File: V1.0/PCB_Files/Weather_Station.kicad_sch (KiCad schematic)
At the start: 39 parts, among them J1 N091-2832TSWFG02-H14, J2 USB_B_Micro, J3 Conn_01x04_Pin, U1 STM32F103C8T6, U2 HDC1080DMBR, U3 AMS1117-3.3, U5 SRV05-4, Y1 X322516MLB4SI

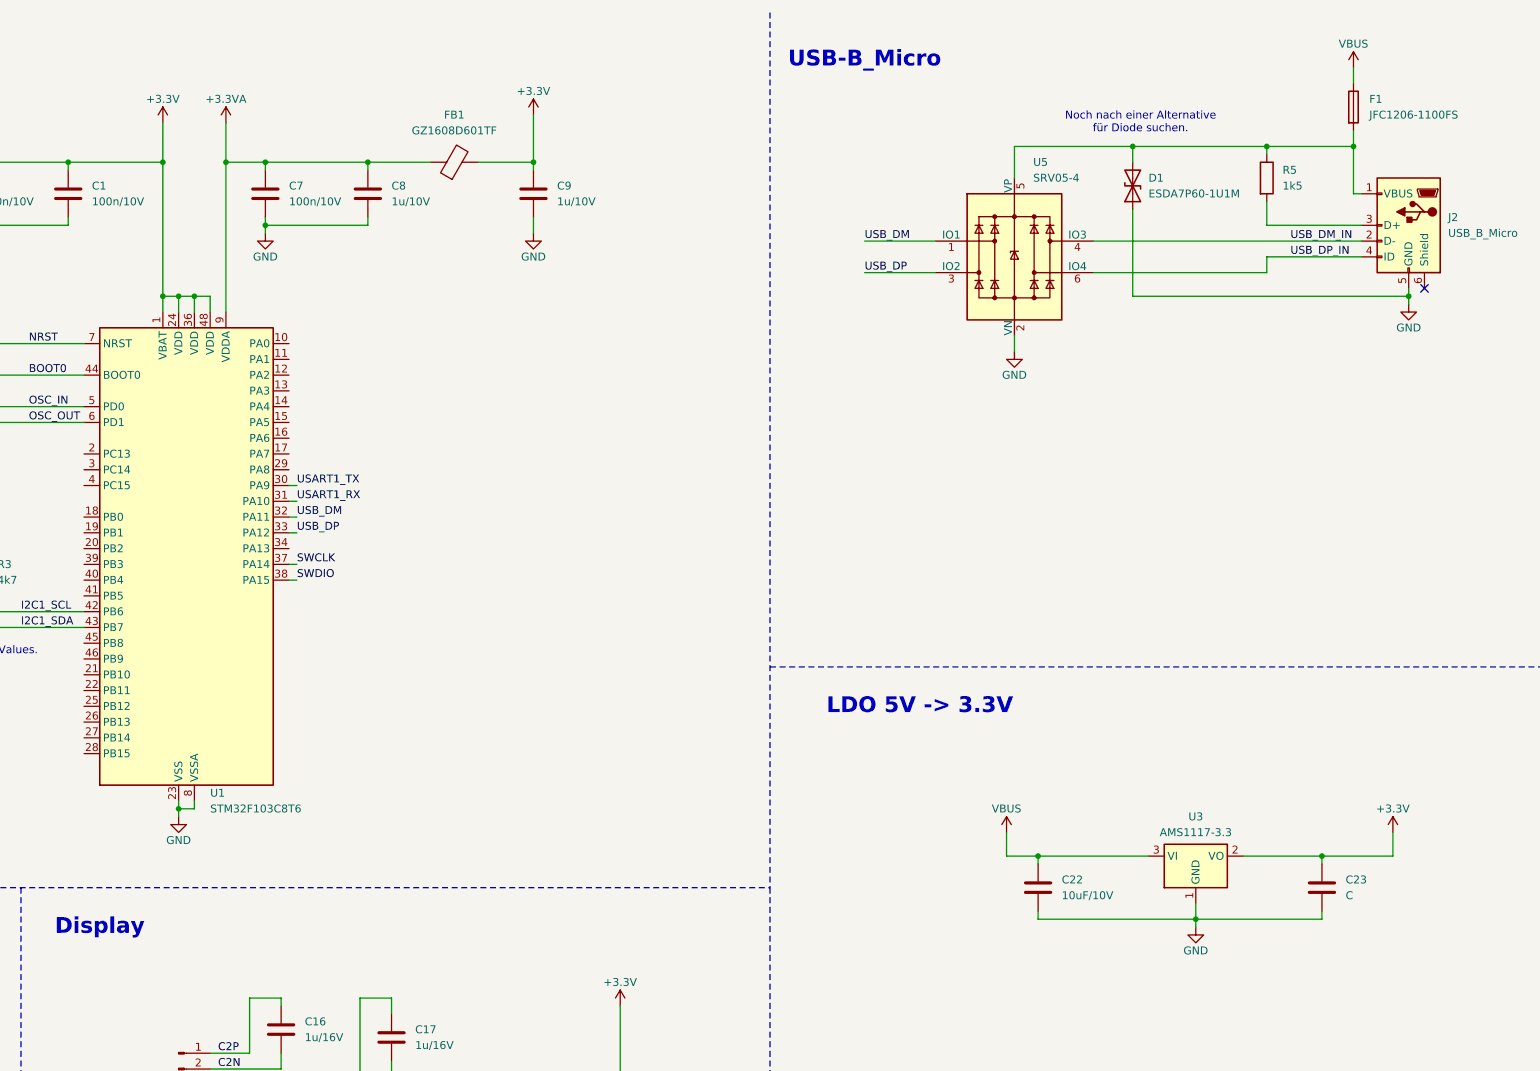
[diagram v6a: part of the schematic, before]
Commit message: Updated Schematic with corrected TVS section.
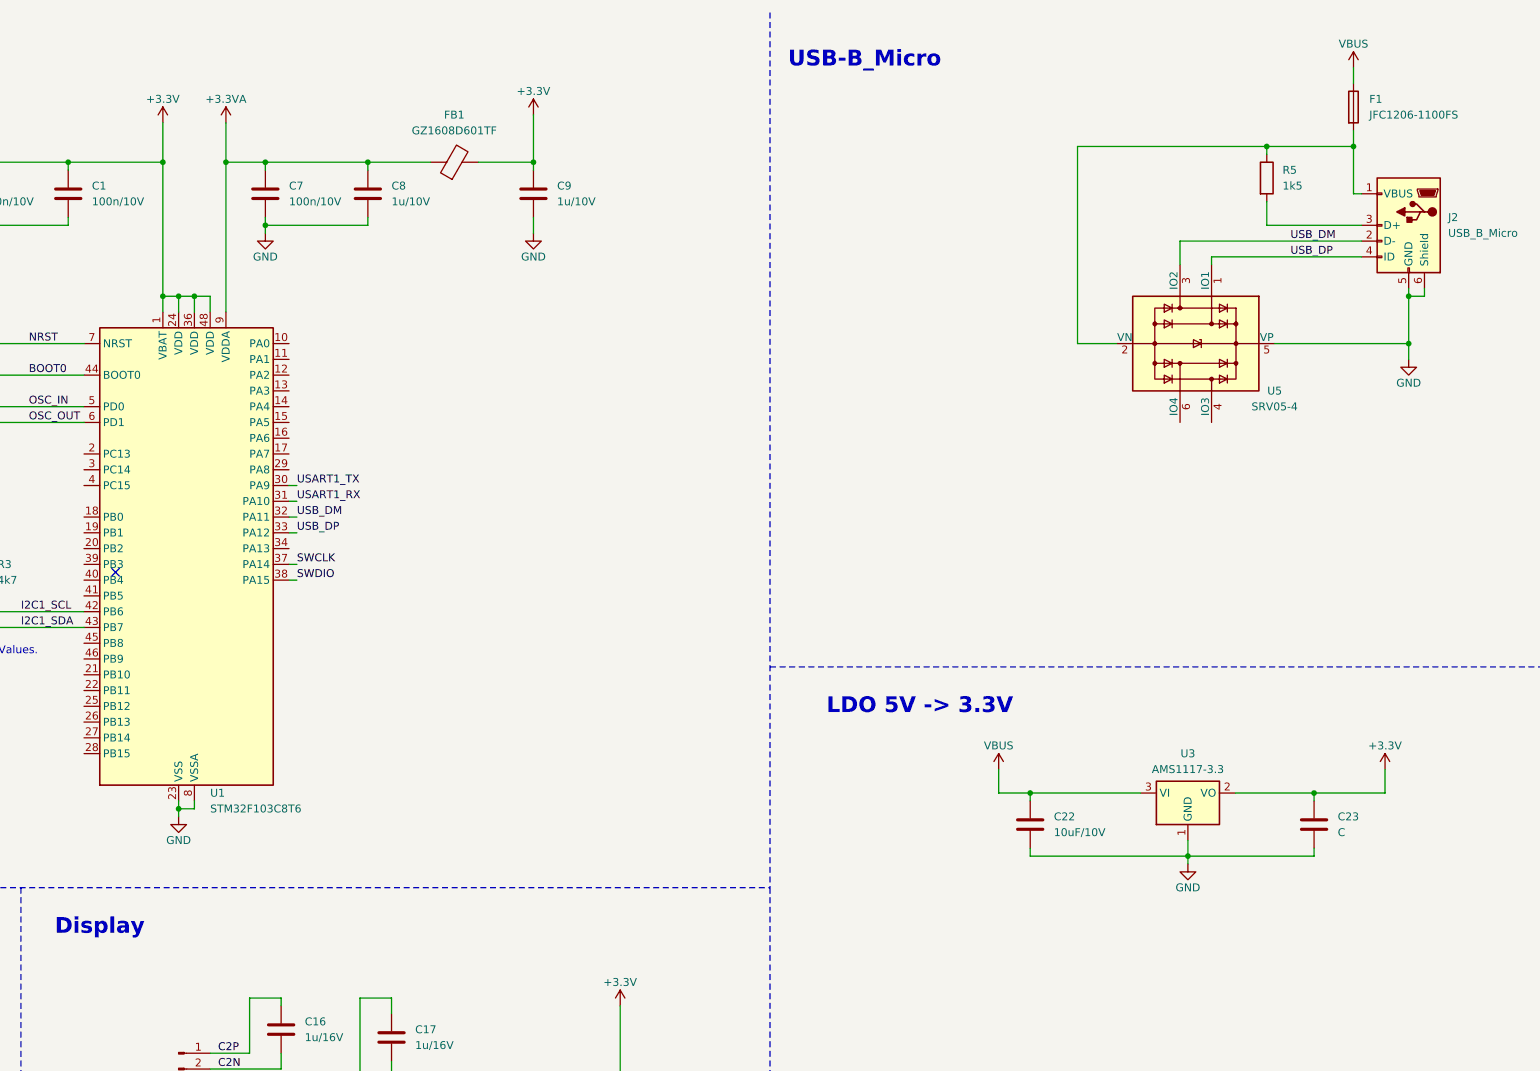
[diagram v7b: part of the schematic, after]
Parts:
- removed D1: ESDA7P60-1U1M, Diode_SMD:ST_QFN-2L_1.6x1.0mm, symbol Device:D_TVS
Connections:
- net GND: now also J2.6 (Shield), U5.5 (VP); no longer U5.2 (VN)
- net USB_DM: now also J2.2 (D-), U5.3 (IO2); no longer U5.1 (IO1)
- net USB_DP: now also J2.4 (ID), U5.1 (IO1); no longer U5.3 (IO2)
- net at F1.2, J2.1 (VBUS), R5.1: now also U5.2 (VN); no longer U5.5 (VP)
- net USB_DM_IN: no longer names the net of U5.4 (IO3)
- net USB_DM_IN: no longer J2.2 (D-)
- net USB_DP_IN: no longer names the net of U5.6 (IO4)
- net USB_DP_IN: no longer J2.4 (ID)
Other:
- note removed: "Noch nach einer Alternative für Diode suchen."
- moved on the sheet: C22, C23, U3, U5

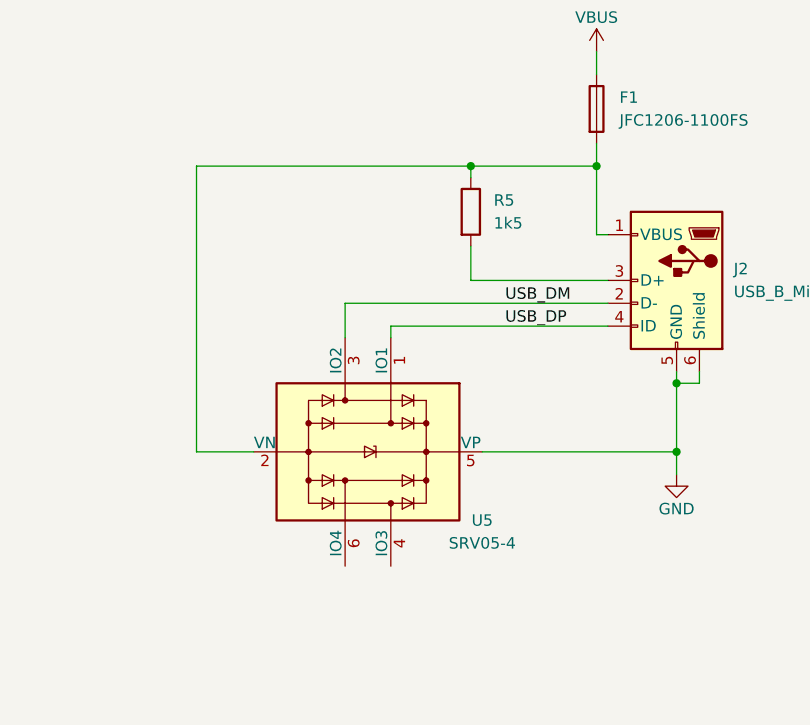
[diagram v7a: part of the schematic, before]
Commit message: Now wiring of USB should be correct.
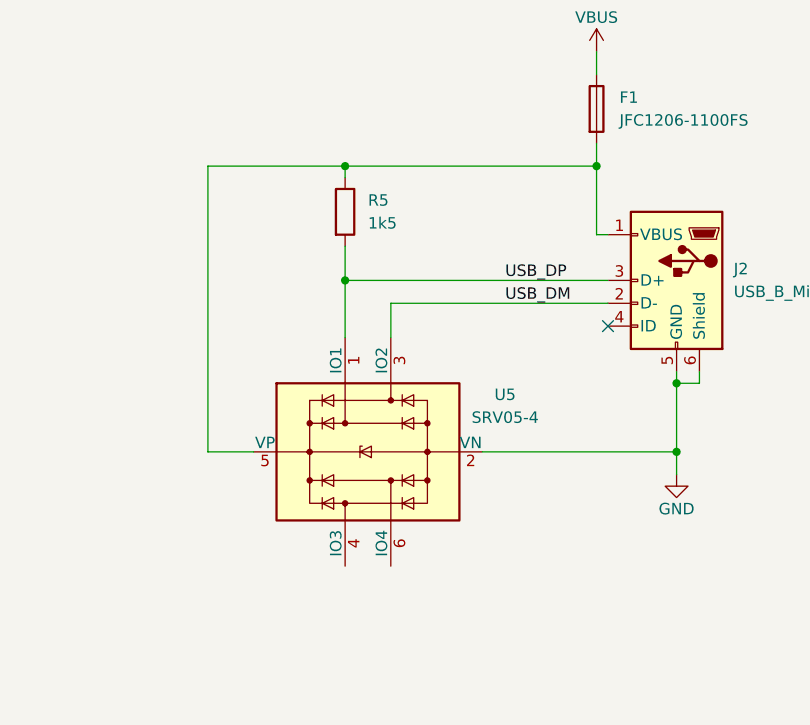
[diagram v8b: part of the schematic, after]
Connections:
- net GND: now also U5.2 (VN); no longer U5.5 (VP)
- net USB_DP: now also J2.3 (D+), R5.2; no longer J2.4 (ID)
- net at F1.2, J2.1 (VBUS), R5.1: now also U5.5 (VP); no longer U5.2 (VN)
- no-connect marks 2 -> 3
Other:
- moved on the sheet: R5, U5
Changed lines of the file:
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@@
 	)
 	(junction
+		(at 290.83 34.29)
+		(diameter 0)
+		(color 0 0 0 0)
+	)
+	(junction
 		(at 63.5 218.44)
 		(diameter 0)
@@
 	)
 	(junction
+		(at 327.66 66.04)
+		(diameter 0)
+		(color 0 0 0 0)
+	)
+	(junction
 		(at 132.08 58.42)
 		(diameter 0)
@@
 	)
 	(junction
-		(at 327.66 66.04)
-		(diameter 0)
-		(color 0 0 0 0)
-	)
-	(junction
 		(at 40.64 46.99)
 		(diameter 0)
@@
 	)
 	(junction
-		(at 304.8 34.29)
-		(diameter 0)
-		(color 0 0 0 0)
-	)
-	(junction
 		(at 143.51 36.83)
 		(diameter 0)
@@
 	)
 	(junction
+		(at 290.83 46.99)
+		(diameter 0)
+		(color 0 0 0 0)
+	)
+	(junction
 		(at 327.66 58.42)
 		(diameter 0)
@@
 	)
 	(no_connect
+		(at 320.04 52.07)
+	)
+	(no_connect
 		(at 119.38 102.87)
 	)
@@
 	(wire
 		(pts
-			(xy 304.8 46.99) (xy 320.04 46.99)
-		)
-		(stroke
-			(width 0)
-			(type default)
-		)
-	)
-	(wire
-		(pts
-			(xy 274.32 66.04) (xy 274.32 34.29)
-		)
-		(stroke
-			(width 0)
-			(type default)
-		)
-	)
-	(wire
-		(pts
 			(xy 140.97 222.25) (xy 140.97 223.52)
 		)
@@
 	(wire
 		(pts
-			(xy 327.66 58.42) (xy 327.66 66.04)
-		)
-		(stroke
-			(width 0)
-			(type default)
-		)
-	)
-	(wire
-		(pts
 			(xy 200.66 224.79) (xy 200.66 223.52)
 		)
@@
 	(wire
 		(pts
-			(xy 274.32 34.29) (xy 304.8 34.29)
+			(xy 76.2 36.83) (xy 76.2 38.1)
 		)
 		(stroke
@@
 	(wire
 		(pts
-			(xy 76.2 36.83) (xy 76.2 38.1)
+			(xy 290.83 46.99) (xy 320.04 46.99)
 		)
 		(stroke
@@
 	(wire
 		(pts
-			(xy 327.66 66.04) (xy 327.66 68.58)
+			(xy 327.66 58.42) (xy 327.66 66.04)
 		)
 		(stroke
@@
 	(wire
 		(pts
-			(xy 24.13 45.72) (xy 24.13 46.99)
+			(xy 275.59 34.29) (xy 290.83 34.29)
 		)
 		(stroke
@@
 	(wire
 		(pts
-			(xy 304.8 34.29) (xy 318.77 34.29)
+			(xy 24.13 45.72) (xy 24.13 46.99)
 		)
 		(stroke
@@
 	(wire
 		(pts
+			(xy 320.04 49.53) (xy 295.91 49.53)
+		)
+		(stroke
+			(width 0)
+			(type default)
+		)
+	)
+	(wire
+		(pts
 			(xy 170.18 190.5) (xy 170.18 191.77)
 		)
@@
 	(wire
 		(pts
-			(xy 295.91 52.07) (xy 320.04 52.07)
+			(xy 306.07 66.04) (xy 327.66 66.04)
 		)
 		(stroke
@@
 	(wire
 		(pts
-			(xy 292.1 148.59) (xy 312.42 148.59)
+			(xy 280.67 66.04) (xy 275.59 66.04)
 		)
 		(stroke
@@
 	(wire
 		(pts
-			(xy 318.77 41.91) (xy 320.04 41.91)
+			(xy 292.1 148.59) (xy 312.42 148.59)
 		)
 		(stroke
@@
 	(wire
 		(pts
-			(xy 266.7 139.7) (xy 266.7 138.43)
+			(xy 318.77 41.91) (xy 320.04 41.91)
 		)
 		(stroke
@@
 	(wire
 		(pts
-			(xy 306.07 66.04) (xy 327.66 66.04)
+			(xy 266.7 139.7) (xy 266.7 138.43)
 		)
 		(stroke
@@
 	(wire
 		(pts
-			(xy 290.83 49.53) (xy 320.04 49.53)
-		)
-		(stroke
-			(width 0)
-			(type default)
-		)
-	)
-	(wire
-		(pts
 			(xy 143.51 46.99) (xy 160.02 46.99)
 		)
@@
 	(wire
 		(pts
-			(xy 304.8 34.29) (xy 304.8 35.56)
+			(xy 290.83 34.29) (xy 290.83 35.56)
 		)
 		(stroke
@@
 	(wire
 		(pts
-			(xy 290.83 49.53) (xy 290.83 53.34)
-		)
-		(stroke
-			(width 0)
-			(type default)
-		)
-	)
-	(wire
-		(pts
 			(xy 59.69 104.14) (xy 82.55 104.14)
 		)
@@
 	(wire
 		(pts
+			(xy 275.59 66.04) (xy 275.59 34.29)
+		)
+		(stroke
+			(width 0)
+			(type default)
+		)
+	)
+	(wire
+		(pts
 			(xy 58.42 36.83) (xy 76.2 36.83)
 		)
@@
 	(wire
 		(pts
-			(xy 280.67 66.04) (xy 274.32 66.04)
+			(xy 295.91 49.53) (xy 295.91 53.34)
 		)
 		(stroke
@@
 	(wire
 		(pts
-			(xy 304.8 43.18) (xy 304.8 46.99)
+			(xy 290.83 43.18) (xy 290.83 46.99)
 		)
 		(stroke
@@
 	(wire
 		(pts
+			(xy 290.83 53.34) (xy 290.83 46.99)
+		)
+		(stroke
+			(width 0)
+			(type default)
+		)
+	)
+	(wire
+		(pts
 			(xy 137.16 198.12) (xy 137.16 190.5)
 		)
@@
 	(wire
 		(pts
+			(xy 290.83 34.29) (xy 318.77 34.29)
+		)
+		(stroke
+			(width 0)
+			(type default)
+		)
+	)
+	(wire
+		(pts
 			(xy 63.5 200.66) (xy 63.5 201.93)
 		)
@@
 	(wire
 		(pts
+			(xy 327.66 66.04) (xy 327.66 68.58)
+		)
+		(stroke
+			(width 0)
+			(type default)
+		)
+	)
+	(wire
+		(pts
 			(xy 41.91 104.14) (xy 41.91 111.76)
 		)
@@
 	(wire
 		(pts
-			(xy 295.91 52.07) (xy 295.91 53.34)
-		)
-		(stroke
-			(width 0)
-			(type default)
-		)
-	)
-	(wire
-		(pts
 			(xy 143.51 46.99) (xy 143.51 48.26)
 		)
@@
 	)
 	(label "USB_DP"
-		(at 308.61 52.07 0)
+		(at 308.61 46.99 0)
 		(fields_autoplaced yes)
 		(effects
@@
 	(symbol
 		(lib_id "Device:R")
-		(at 304.8 39.37 0)
+		(at 290.83 39.37 0)
 		(unit 1)
 		(exclude_from_sim no)
@@
 		(fields_autoplaced yes)
 		(property "Reference" "R5"
-			(at 307.34 38.0999 0)
+			(at 293.37 38.0999 0)
 			(effects
 				(font
@@
 		)
 		(property "Value" "1k5"
-			(at 307.34 40.6399 0)
+			(at 293.37 40.6399 0)
 			(effects
 				(font
@@
 		)
 		(property "Footprint" "Resistor_SMD:R_0603_1608Metric"
-			(at 303.022 39.37 90)
+			(at 289.052 39.37 90)
 			(effects
 				(font
@@
 		)
 		(property "Datasheet" "~"
-			(at 304.8 39.37 0)
+			(at 290.83 39.37 0)
 			(effects
 				(font
@@
 		)
 		(property "Description" "Resistor"
-			(at 304.8 39.37 0)
+			(at 290.83 39.37 0)
 			(effects
 				(font
@@
 	(symbol
 		(lib_id "Power_Protection:SRV05-4")
-		(at 293.37 66.04 270)
+		(at 293.37 66.04 90)
+		(mirror x)
 		(unit 1)
 		(exclude_from_sim no)
@@
 		(dnp no)
 		(property "Reference" "U5"
-			(at 306.07 73.66 90)
+			(at 308.61 59.69 90)
 			(effects
 				(font
@@
 		)
 		(property "Value" "SRV05-4"
-			(at 306.07 76.2 90)
+			(at 308.61 62.23 90)
 			(effects
 				(font
@@
 		)
 		(property "Footprint" "Package_TO_SOT_SMD:SOT-23-6"
-			(at 281.94 83.82 0)
+			(at 304.8 83.82 0)
 			(effects
 				(font
